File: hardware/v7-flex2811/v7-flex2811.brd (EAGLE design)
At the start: 7 x 7 mm, 6 parts, among them IC1 WS2811-SOP8

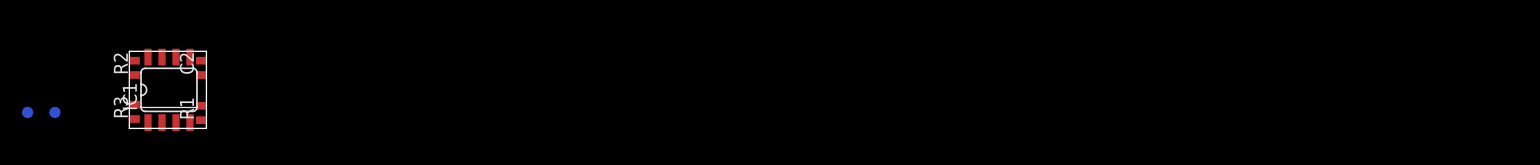
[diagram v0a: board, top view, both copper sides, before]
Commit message: first draft tapper strip
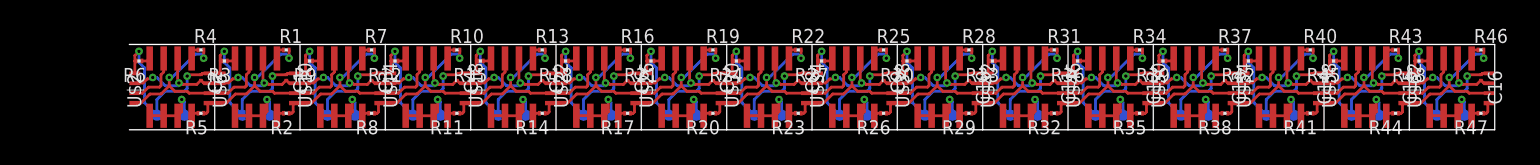
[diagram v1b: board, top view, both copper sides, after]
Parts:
- removed IC1: WS2811-SOP8, adafruit:SO08-SKINNYPADS
- added C1, C10, C11, C12, C13, C14, C15, C16, C3, C4, C5, C6, C7, C8, C9: (no value), rcl:C0201
- added R10, R11, R12, R13, R14, R15, R16, R17, R18, R19, R20, R21, R22, R23, R24, R25, R26, R27, R28, R29, R30, R31, R32, R33, R34, R35, R36, R37, R38, R39, R4, R40, R41, R42, R43, R44, R45, R46, R47, R48, R5, R6, R7, R8, R9: (no value), rcl:R0201
- added U$10, U$14, U$18, U$2, U$22, U$26, U$30, U$34, U$38, U$42, U$46, U$50, U$54, U$58, U$6, U$62: WS2818, adafruit:SO08
- added U$11, U$12, U$15, U$16, U$19, U$20, U$23, U$24, U$27, U$28, U$3, U$31, U$32, U$35, U$36, U$39, U$4, U$40, U$43, U$44, U$47, U$48, U$51, U$52, U$55, U$56, U$59, U$60, U$63, U$64, U$7, U$8: 4PAD, Sparky:4PAD
- added U$13, U$17, U$21, U$25, U$29, U$33, U$37, U$41, U$45, U$49, U$5, U$53, U$57, U$61, U$9: TP_4MM_MED_PAD, tom-tappytap-v5-flex:TP_4MM_MED_PAD
- C2: device rcl:C0402 -> rcl:C0201
- R1, R2, R3: device rcl:R0402 -> rcl:R0201
- moved R2 14.4 mm to (14.2, 1.38), turned to 180 degrees
- moved U$1 11.8 mm to (3.75, 3.75)
- moved R1 9.64 mm to (14.2, 7.12), turned to 0 degrees
- moved R3 9.35 mm to (8.62, 6.12), turned to 180 degrees
- moved C2 0.88 mm to (6.50, 4.62), turned to 270 degrees
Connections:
- new net BIN: U$10.7, U$11.P$2, U$14.7, U$15.P$2, U$18.7, U$19.P$2, U$2.7, U$22.7, U$23.P$2, U$26.7, U$27.P$2, U$3.P$2, U$30.7, U$31.P$2, U$34.7, U$35.P$2, U$38.7, U$39.P$2, U$42.7, U$43.P$2, U$46.7, U$47.P$2, U$50.7, U$51.P$2, U$54.7, U$55.P$2, U$58.7, U$59.P$2, U$6.7, U$62.7, U$63.P$2, U$7.P$2
- new net N$10: R10.1, U$14.5
- new net N$11: R11.2, U$14.4
- new net N$12: R12.1, U$14.8
- new net N$13: R13.1, U$18.5
- new net N$14: R14.2, U$18.4
- new net N$15: R15.1, U$18.8
- new net N$16: R16.1, U$22.5
- new net N$17: R17.2, U$22.4
- new net N$18: R18.1, U$22.8
- new net N$19: R19.1, U$26.5
- new net N$20: R20.2, U$26.4
- new net N$21: R21.1, U$26.8
- new net N$22: R22.1, U$30.5
- new net N$23: R23.2, U$30.4
- new net N$24: R24.1, U$30.8
- new net N$25: R25.1, U$34.5
- new net N$26: R26.2, U$34.4
- new net N$27: R27.1, U$34.8
- new net N$28: R28.1, U$38.5
- new net N$29: R29.2, U$38.4
- new net N$30: R30.1, U$38.8
- new net N$31: R31.1, U$42.5
- new net N$32: R32.2, U$42.4
- new net N$33: R33.1, U$42.8
- new net N$34: R34.1, U$46.5
- new net N$35: R35.2, U$46.4
- new net N$36: R36.1, U$46.8
- new net N$37: R37.1, U$50.5
- new net N$38: R38.2, U$50.4
- new net N$39: R39.1, U$50.8
- new net N$4: R4.1, U$2.5
- new net N$40: R40.1, U$54.5
- new net N$41: R41.2, U$54.4
- new net N$42: R42.1, U$54.8
- new net N$43: R43.1, U$58.5
- new net N$44: R44.2, U$58.4
- new net N$45: R45.1, U$58.8
- new net N$46: R46.1, U$62.5
- new net N$47: R47.2, U$62.4
- new net N$48: R48.1, U$62.8
- new net N$5: R5.2, U$2.4
- new net N$6: R6.1, U$2.8
- new net N$7: R7.1, U$10.5
- new net N$8: R8.2, U$10.4
- new net N$9: R9.1, U$10.8
- net DIN: now also R1.2, R10.2, R13.2, R16.2, R19.2, R22.2, R25.2, R28.2, R31.2, R34.2, R37.2, R4.2, R40.2, R43.2, R46.2, R7.2, U$11.P$1, U$12.P$2, U$15.P$1, U$16.P$2, U$19.P$1, U$20.P$2, U$23.P$1, U$24.P$2, U$27.P$1, U$28.P$2, U$3.P$1, U$31.P$1, U$32.P$2, U$35.P$1, U$36.P$2, U$39.P$1, U$4.P$2, U$40.P$2, U$43.P$1, U$44.P$2, U$47.P$1, U$48.P$2, U$51.P$1, U$52.P$2, U$55.P$1, U$56.P$2, U$59.P$1, U$60.P$2, U$63.P$1, U$64.P$2, U$7.P$1, U$8.P$2; no longer R2.2
- net DOUT: now also R11.1, R14.1, R17.1, R2.1, R20.1, R23.1, R26.1, R29.1, R32.1, R35.1, R38.1, R41.1, R44.1, R47.1, R5.1, R8.1, U$12.P$1, U$16.P$1, U$20.P$1, U$24.P$1, U$28.P$1, U$32.P$1, U$36.P$1, U$4.P$1, U$40.P$1, U$44.P$1, U$48.P$1, U$52.P$1, U$56.P$1, U$60.P$1, U$64.P$1, U$8.P$1; no longer R3.2
- net GND: now also C1.2, C10.2, C11.2, C12.2, C13.2, C14.2, C15.2, C16.2, C3.2, C4.2, C5.2, C6.2, C7.2, C8.2, C9.2, U$10.6, U$11.P$3, U$12.P$3, U$14.6, U$15.P$3, U$16.P$3, U$18.6, U$19.P$3, U$2.6, U$20.P$3, U$22.6, U$23.P$3, U$24.P$3, U$26.6, U$27.P$3, U$28.P$3, U$3.P$3, U$30.6, U$31.P$3, U$32.P$3, U$34.6, U$35.P$3, U$36.P$3, U$38.6, U$39.P$3, U$4.P$3, U$40.P$3, U$42.6, U$43.P$3, U$44.P$3, U$46.6, U$47.P$3, U$48.P$3, U$50.6, U$51.P$3, U$52.P$3, U$54.6, U$55.P$3, U$56.P$3, U$58.6, U$59.P$3, U$6.6, U$60.P$3, U$62.6, U$63.P$3, U$64.P$3, U$7.P$3, U$8.P$3; no longer IC1.4
- net N$1: now also U$6.5; no longer IC1.8
- net N$2: now also R2.2, U$6.4; no longer IC1.6, R2.1
- net N$3: now also U$6.8; no longer IC1.5
- net NEG_PAD: now also U$10.1, U$10.2, U$10.3, U$13.P$1, U$14.1, U$14.2, U$14.3, U$17.P$1, U$18.1, U$18.2, U$18.3, U$2.1, U$2.2, U$2.3, U$21.P$1, U$22.1, U$22.2, U$22.3, U$25.P$1, U$26.1, U$26.2, U$26.3, U$29.P$1, U$30.1, U$30.2, U$30.3, U$33.P$1, U$34.1, U$34.2, U$34.3, U$37.P$1, U$38.1, U$38.2, U$38.3, U$41.P$1, U$42.1, U$42.2, U$42.3, U$45.P$1, U$46.1, U$46.2, U$46.3, U$49.P$1, U$5.P$1, U$50.1, U$50.2, U$50.3, U$53.P$1, U$54.1, U$54.2, U$54.3, U$57.P$1, U$58.1, U$58.2, U$58.3, U$6.1, U$6.2, U$6.3, U$61.P$1, U$62.1, U$62.2, U$62.3, U$9.P$1; no longer IC1.1, IC1.2, IC1.3
- net VCC: now also C1.1, C10.1, C11.1, C12.1, C13.1, C14.1, C15.1, C16.1, C3.1, C4.1, C5.1, C6.1, C7.1, C8.1, C9.1, R12.2, R15.2, R18.2, R21.2, R24.2, R27.2, R3.2, R30.2, R33.2, R36.2, R39.2, R42.2, R45.2, R48.2, R6.2, R9.2, U$11.P$4, U$12.P$4, U$13.P$2, U$15.P$4, U$16.P$4, U$17.P$2, U$19.P$4, U$20.P$4, U$21.P$2, U$23.P$4, U$24.P$4, U$25.P$2, U$27.P$4, U$28.P$4, U$29.P$2, U$3.P$4, U$31.P$4, U$32.P$4, U$33.P$2, U$35.P$4, U$36.P$4, U$37.P$2, U$39.P$4, U$4.P$4, U$40.P$4, U$41.P$2, U$43.P$4, U$44.P$4, U$45.P$2, U$47.P$4, U$48.P$4, U$49.P$2, U$5.P$2, U$51.P$4, U$52.P$4, U$53.P$2, U$55.P$4, U$56.P$4, U$57.P$2, U$59.P$4, U$60.P$4, U$61.P$2, U$63.P$4, U$64.P$4, U$7.P$4, U$8.P$4, U$9.P$2; no longer R1.2
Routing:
- net VCC: track 0.00 -> 265.2 mm, vias 0 -> 32
- net DIN: track 0.00 -> 217.0 mm, vias 0 -> 32
- net GND: track 0.00 -> 162.5 mm, vias 0 -> 32
- net NEG_PAD: track 0.00 -> 91.0 mm, vias 0 -> 16
- net BIN: track 0.00 -> 83.8 mm
- net DOUT: track 0.00 -> 20.4 mm
- net N$46: track 0.00 -> 1.56 mm
- net N$43: track 0.00 -> 1.56 mm
- net N$40: track 0.00 -> 1.56 mm
- net N$37: track 0.00 -> 1.56 mm
- net N$34: track 0.00 -> 1.56 mm
- net N$31: track 0.00 -> 1.56 mm
- net N$28: track 0.00 -> 1.56 mm
- net N$25: track 0.00 -> 1.56 mm
- net N$7: track 0.00 -> 1.56 mm
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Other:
- board size 7 x 7 mm -> 124 x 7.8 mm
